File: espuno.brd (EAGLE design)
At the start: 68.6 x 53.3 mm, 62 parts, among them IC1 REG1117, J1 ARDUINO_R3_SHIELD, T1 FDN340P, U1 ADS1015, U2 NCP1117ST50T3G, U3 CAT9532WI, U4 FT232R, U5 LMV358IDGKR, U6 MCP73831, U7 TPS61200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

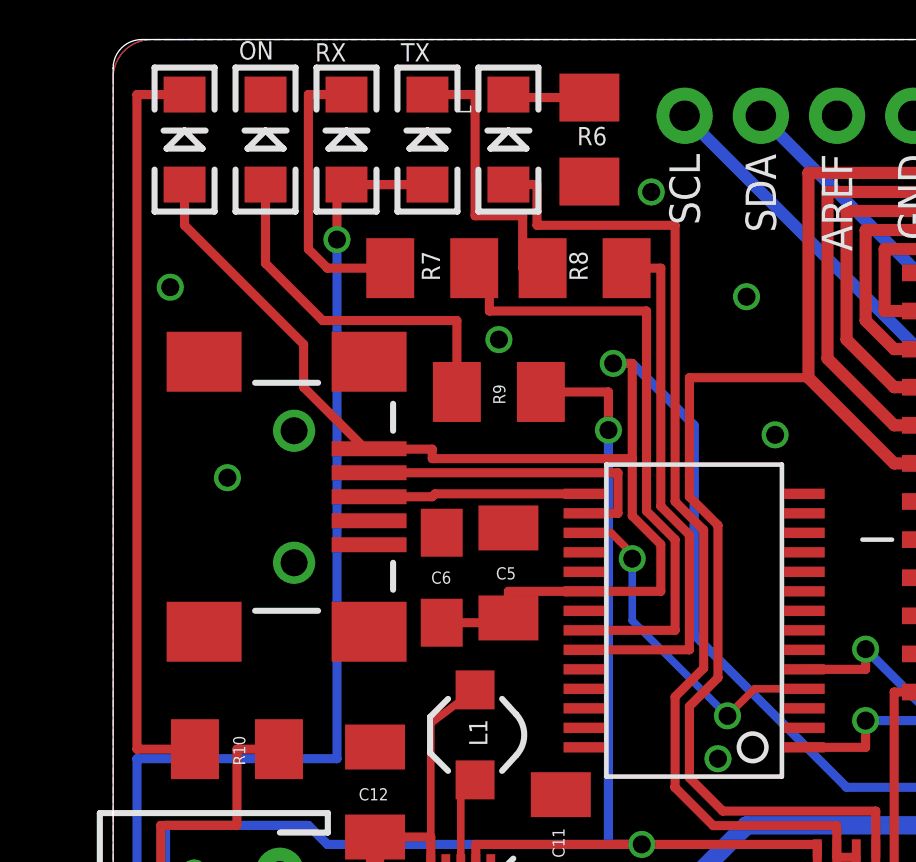
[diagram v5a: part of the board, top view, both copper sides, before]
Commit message: Add 500mA fuse
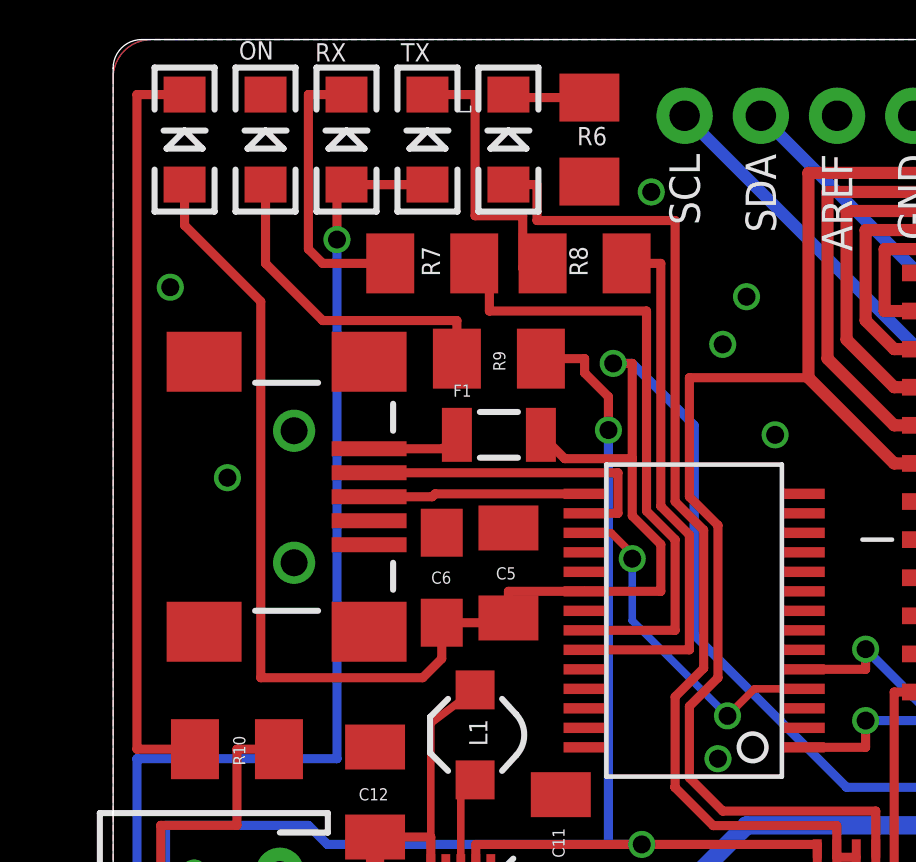
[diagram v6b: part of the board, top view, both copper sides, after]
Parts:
- added F1: 500mA, SparkFun:PTC-1206
- moved R9 1.11 mm to (12.9, 42.7)
- moved R7 0.16 mm to (10.6, 45.9)
- moved R8 0.16 mm to (15.7, 45.9)
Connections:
- new net VBUS: F1.1, JP1.VBUS
- net USBVCC: now also F1.2; no longer JP1.VBUS
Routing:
- net USBVCC: track 90.9 -> 98.7 mm
- net VBUS: track 0.00 -> 3.12 mm
- net N$1: track 12.2 -> 11.1 mm
- net 5V: track 181.4 -> 182.0 mm
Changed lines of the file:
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@@
 <attribute name="NAME" x="15.46225" y="49.81575" size="0.6096" layer="25" font="vector"/>
 </element>
-<element name="R9" library="rcl" package="M1206" value="470" x="12.85875" y="41.5925" smashed="yes" rot="R180">
-<attribute name="NAME" x="12.66825" y="41.8465" size="0.4064" layer="25" font="vector" rot="R270"/>
+<element name="R9" library="rcl" package="M1206" value="470" x="12.85875" y="42.70375" smashed="yes" rot="R180">
+<attribute name="NAME" x="12.66825" y="42.95775" size="0.4064" layer="25" font="vector" rot="R270"/>
 </element>
 <element name="X1" library="SmartPrj" package="POWERSUPPLY_DC-21MM" value="POWERSUPPLY_DC21MMX" x="2.06375" y="8.41375" smashed="yes" rot="R90"/>
@@
 <attribute name="VALUE" x="18.4714125" y="36.408221875" size="1.016" layer="27" rot="R270"/>
 </element>
-<element name="R7" library="rcl" package="M1206" value="330" x="10.63625" y="45.72" smashed="yes" rot="R180">
-<attribute name="NAME" x="10.287" y="46.2915" size="0.6096" layer="25" font="vector" rot="R270"/>
-</element>
-<element name="R8" library="rcl" package="M1206" value="330" x="15.71625" y="45.72" smashed="yes" rot="R180">
-<attribute name="NAME" x="15.20825" y="46.2915" size="0.6096" layer="25" font="vector" rot="R270"/>
+<element name="R7" library="rcl" package="M1206" value="330" x="10.63625" y="45.87875" smashed="yes" rot="R180">
+<attribute name="NAME" x="10.287" y="46.45025" size="0.6096" layer="25" font="vector" rot="R270"/>
+</element>
+<element name="R8" library="rcl" package="M1206" value="330" x="15.71625" y="45.87875" smashed="yes" rot="R180">
+<attribute name="NAME" x="15.20825" y="46.45025" size="0.6096" layer="25" font="vector" rot="R270"/>
 </element>
 <element name="RX" library="SparkFun-LED" package="LED-1206" value="GREEN" x="7.77875" y="50.00625" smashed="yes" rot="R90">
@@
 <attribute name="PROD_ID" value="IC-12239" x="50.165" y="13.97" size="1.778" layer="27" display="off"/>
 </element>
+<element name="F1" library="SparkFun" package="PTC-1206" value="500mA" x="12.85875" y="40.16375"/>
 </elements>
 <signals>
@@
 <via x="3.81" y="38.735" extent="1-16" drill="0.6"/>
 <via x="1.905" y="45.085" extent="1-16" drill="0.6"/>
-<via x="12.85875" y="43.33875" extent="1-16" drill="0.6"/>
+<via x="20.32" y="43.18" extent="1-16" drill="0.6"/>
 <via x="22.70125" y="3.175" extent="1-16" drill="0.6"/>
 <via x="48.26" y="2.69875" extent="1-16" drill="0.6"/>
@@
 <wire x1="12.08875" y1="25.76375" x2="12.08875" y2="26.51125" width="0.3048" layer="1"/>
 <wire x1="12.08875" y1="26.51125" x2="17.62125" y2="26.51125" width="0.3048" layer="1"/>
-<wire x1="14.25875" y1="41.5925" x2="16.51" y2="41.5925" width="0.3048" layer="1"/>
-<wire x1="16.51" y1="41.5925" x2="16.51" y2="40.3225" width="0.3048" layer="1"/>
+<wire x1="14.25875" y1="42.70375" x2="15.71625" y2="42.70375" width="0.3048" layer="1"/>
+<wire x1="15.71625" y1="42.70375" x2="15.71625" y2="42.2275" width="0.3048" layer="1"/>
+<wire x1="15.71625" y1="42.2275" x2="16.51" y2="41.43375" width="0.3048" layer="1"/>
+<wire x1="16.51" y1="41.43375" x2="16.51" y2="40.3225" width="0.3048" layer="1"/>
 <via x="16.51" y="40.3225" extent="1-16" drill="0.6" shape="square"/>
 <wire x1="16.51" y1="40.3225" x2="16.51" y2="26.51125" width="0.3048" layer="16"/>
@@
 <contactref element="ON" pad="A"/>
 <contactref element="R9" pad="2"/>
-<wire x1="11.45875" y1="41.5925" x2="11.45875" y2="43.97375" width="0.3048" layer="1"/>
+<wire x1="11.45875" y1="42.70375" x2="11.45875" y2="43.97375" width="0.3048" layer="1"/>
 <wire x1="11.45875" y1="43.97375" x2="6.985" y2="43.97375" width="0.3048" layer="1"/>
 <wire x1="5.08" y1="48.50625" x2="5.08" y2="45.87875" width="0.3048" layer="1"/>
@@
 <contactref element="C9" pad="1"/>
 <contactref element="D4" pad="A"/>
-<contactref element="JP1" pad="VBUS"/>
 <wire x1="15.7115" y1="34.9475" x2="18.25625" y2="34.9475" width="0.3048" layer="1"/>
 <wire x1="18.25625" y1="34.9475" x2="18.25625" y2="36.5125" width="0.3048" layer="1"/>
 <wire x1="18.25625" y1="36.5125" x2="17.30375" y2="37.465" width="0.3048" layer="1"/>
-<wire x1="17.30375" y1="37.465" x2="17.30375" y2="39.37" width="0.3048" layer="1"/>
-<wire x1="17.30375" y1="39.37" x2="10.63625" y2="39.37" width="0.3048" layer="1"/>
-<wire x1="10.63625" y1="39.37" x2="10.63625" y2="39.6875" width="0.3048" layer="1"/>
-<wire x1="10.63625" y1="39.6875" x2="8.5325" y2="39.6875" width="0.3048" layer="1"/>
-<wire x1="8.5325" y1="39.6875" x2="8.5325" y2="39.7" width="0.3048" layer="1"/>
 <wire x1="15.7115" y1="34.9475" x2="13.17625" y2="34.9475" width="0.3048" layer="1"/>
 <wire x1="13.17625" y1="34.9475" x2="13.17625" y2="34.06" width="0.3048" layer="1"/>
 <wire x1="10.95375" y1="33.90125" x2="13.17625" y2="33.90125" width="0.3048" layer="1"/>
 <wire x1="13.17625" y1="33.90125" x2="13.17625" y2="34.06" width="0.3048" layer="1"/>
-<wire x1="8.5325" y1="39.7" x2="8.40125" y2="39.7" width="0.3048" layer="1"/>
-<wire x1="8.40125" y1="39.7" x2="6.35" y2="41.75125" width="0.3048" layer="1"/>
-<wire x1="6.35" y1="41.75125" x2="6.35" y2="43.18" width="0.3048" layer="1"/>
-<wire x1="6.35" y1="43.18" x2="2.38125" y2="47.14875" width="0.3048" layer="1"/>
 <wire x1="2.38125" y1="47.14875" x2="2.38125" y2="48.50625" width="0.3048" layer="1"/>
 <wire x1="31.0275" y1="14.2875" x2="29.68625" y2="14.2875" width="0.3048" layer="1"/>
@@
 <wire x1="16.66875" y1="42.545" x2="17.30375" y2="42.545" width="0.3048" layer="1"/>
 <wire x1="17.30375" y1="42.545" x2="17.30375" y2="39.37" width="0.3048" layer="1"/>
+<contactref element="F1" pad="2"/>
+<wire x1="17.30375" y1="39.37" x2="17.30375" y2="37.465" width="0.3048" layer="1"/>
+<wire x1="14.25875" y1="40.16375" x2="15.0525" y2="39.37" width="0.3048" layer="1"/>
+<wire x1="15.0525" y1="39.37" x2="17.30375" y2="39.37" width="0.3048" layer="1"/>
+<wire x1="2.38125" y1="47.14875" x2="4.92125" y2="44.60875" width="0.3048" layer="1"/>
+<wire x1="4.92125" y1="44.60875" x2="4.92125" y2="32.0675" width="0.3048" layer="1"/>
+<wire x1="4.92125" y1="32.0675" x2="10.31875" y2="32.0675" width="0.3048" layer="1"/>
+<wire x1="10.31875" y1="32.0675" x2="10.95375" y2="32.7025" width="0.3048" layer="1"/>
+<wire x1="10.95375" y1="32.7025" x2="10.95375" y2="33.90125" width="0.3048" layer="1"/>
 </signal>
 <signal name="L13">
@@
 <contactref element="L" pad="A"/>
 <wire x1="13.17625" y1="48.50625" x2="14.12875" y2="48.50625" width="0.3048" layer="1"/>
-<wire x1="14.12875" y1="48.50625" x2="14.12875" y2="47.14875" width="0.3048" layer="1"/>
-<wire x1="14.12875" y1="47.14875" x2="18.7325" y2="47.14875" width="0.3048" layer="1"/>
-<wire x1="18.7325" y1="47.14875" x2="18.7325" y2="37.94125" width="0.3048" layer="1"/>
+<wire x1="14.12875" y1="48.50625" x2="14.12875" y2="47.3075" width="0.3048" layer="1"/>
+<wire x1="14.12875" y1="47.3075" x2="18.7325" y2="47.3075" width="0.3048" layer="1"/>
+<wire x1="18.7325" y1="47.3075" x2="18.7325" y2="37.94125" width="0.3048" layer="1"/>
 <wire x1="18.7325" y1="37.94125" x2="19.685" y2="36.98875" width="0.3048" layer="1"/>
 <wire x1="19.685" y1="36.98875" x2="19.685" y2="32.385" width="0.3048" layer="1"/>
@@
 <contactref element="RX" pad="C"/>
 <contactref element="R7" pad="2"/>
-<wire x1="9.23625" y1="45.72" x2="7.14375" y2="45.72" width="0.3048" layer="1"/>
-<wire x1="7.14375" y1="45.72" x2="6.50875" y2="46.355" width="0.3048" layer="1"/>
+<wire x1="9.23625" y1="45.87875" x2="6.985" y2="45.87875" width="0.3048" layer="1"/>
+<wire x1="6.985" y1="45.87875" x2="6.50875" y2="46.355" width="0.3048" layer="1"/>
 <wire x1="7.77875" y1="51.50625" x2="6.50875" y2="51.50625" width="0.3048" layer="1"/>
 <wire x1="6.50875" y1="51.50625" x2="6.50875" y2="46.355" width="0.3048" layer="1"/>
@@
 <contactref element="TX" pad="C"/>
 <contactref element="R8" pad="2"/>
-<wire x1="14.31625" y1="45.72" x2="13.6525" y2="45.72" width="0.3048" layer="1"/>
+<wire x1="14.31625" y1="45.87875" x2="13.6525" y2="45.72" width="0.3048" layer="1"/>
 <wire x1="13.6525" y1="45.72" x2="13.6525" y2="47.46625" width="0.3048" layer="1"/>
 <wire x1="13.6525" y1="47.46625" x2="12.065" y2="47.46625" width="0.3048" layer="1"/>
@@
 <contactref element="U4" pad="22"/>
 <contactref element="R7" pad="1"/>
-<wire x1="12.03625" y1="45.72" x2="12.03625" y2="45.56125" width="0.3048" layer="1"/>
+<wire x1="12.03625" y1="45.87875" x2="12.03625" y2="45.56125" width="0.3048" layer="1"/>
 <wire x1="12.03625" y1="45.56125" x2="12.54125" y2="45.56125" width="0.3048" layer="1"/>
 <wire x1="12.54125" y1="45.56125" x2="12.54125" y2="44.29125" width="0.3048" layer="1"/>
@@
 <contactref element="R8" pad="1"/>
 <contactref element="U4" pad="23"/>
-<wire x1="17.11625" y1="45.72" x2="16.9575" y2="45.72" width="0.3048" layer="1"/>
-<wire x1="17.11625" y1="45.72" x2="18.25625" y2="45.72" width="0.3048" layer="1"/>
-<wire x1="18.25625" y1="45.72" x2="18.25625" y2="37.7825" width="0.3048" layer="1"/>
+<wire x1="17.11625" y1="45.87875" x2="16.9575" y2="45.72" width="0.3048" layer="1"/>
+<wire x1="17.11625" y1="45.87875" x2="18.25625" y2="45.87875" width="0.3048" layer="1"/>
+<wire x1="18.25625" y1="45.87875" x2="18.25625" y2="37.7825" width="0.3048" layer="1"/>
 <wire x1="18.25625" y1="37.7825" x2="19.20875" y2="36.83" width="0.3048" layer="1"/>
 <wire x1="19.20875" y1="36.83" x2="19.20875" y2="32.9975" width="0.3048" layer="1"/>
@@
 <wire x1="21.37875" y1="31.6975" x2="23.0235" y2="31.6975" width="0.254" layer="1"/>
 </signal>
+<signal name="VBUS">
+<contactref element="F1" pad="1"/>
+<contactref element="JP1" pad="VBUS"/>
+<wire x1="11.45875" y1="40.16375" x2="10.995" y2="39.7" width="0.3048" layer="1"/>
+<wire x1="10.995" y1="39.7" x2="8.5325" y2="39.7" width="0.3048" layer="1"/>
+</signal>
 </signals>
